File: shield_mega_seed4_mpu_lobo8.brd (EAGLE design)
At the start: 99.4 x 72.4 mm, 37 parts, among them U1 GY-521MPU6050

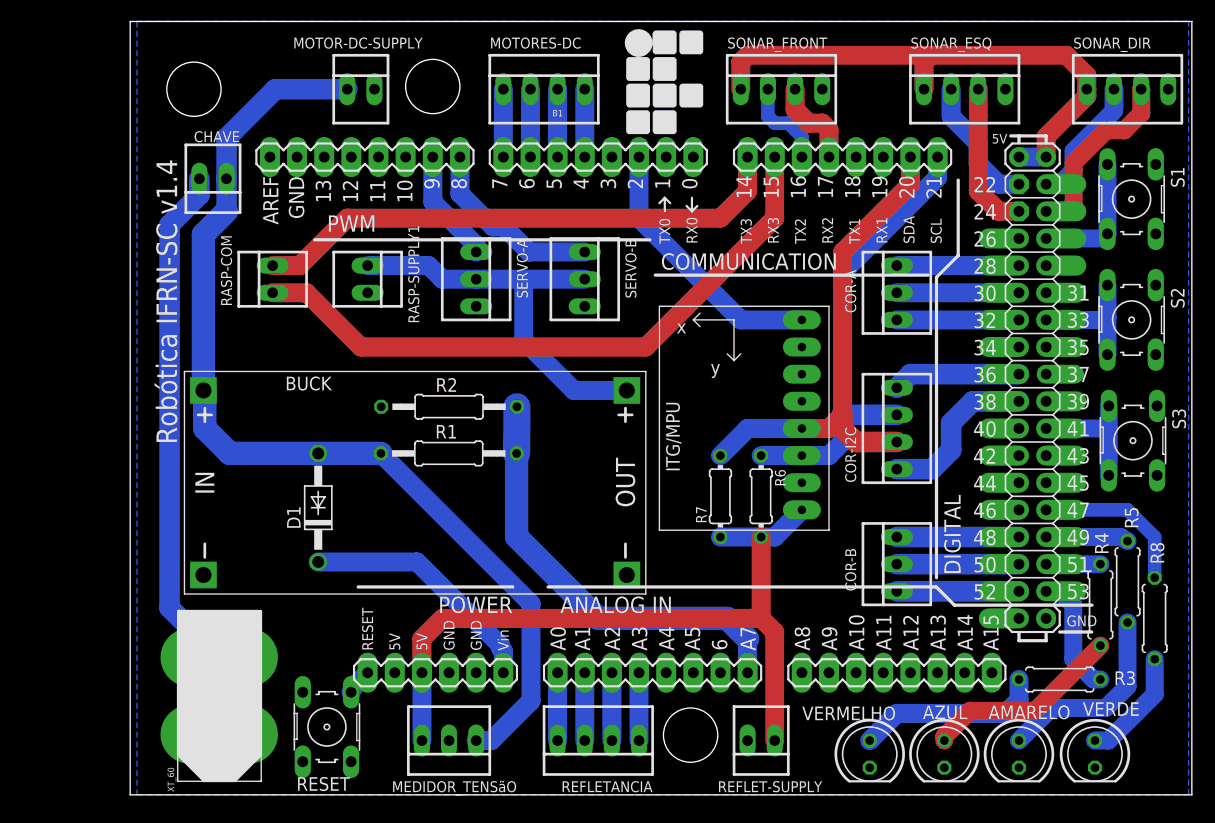
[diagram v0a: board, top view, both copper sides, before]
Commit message: Adição de módulo bluetooth; Remoção do buck; Remoção de conector XT-60; Remoção de conector da chave;
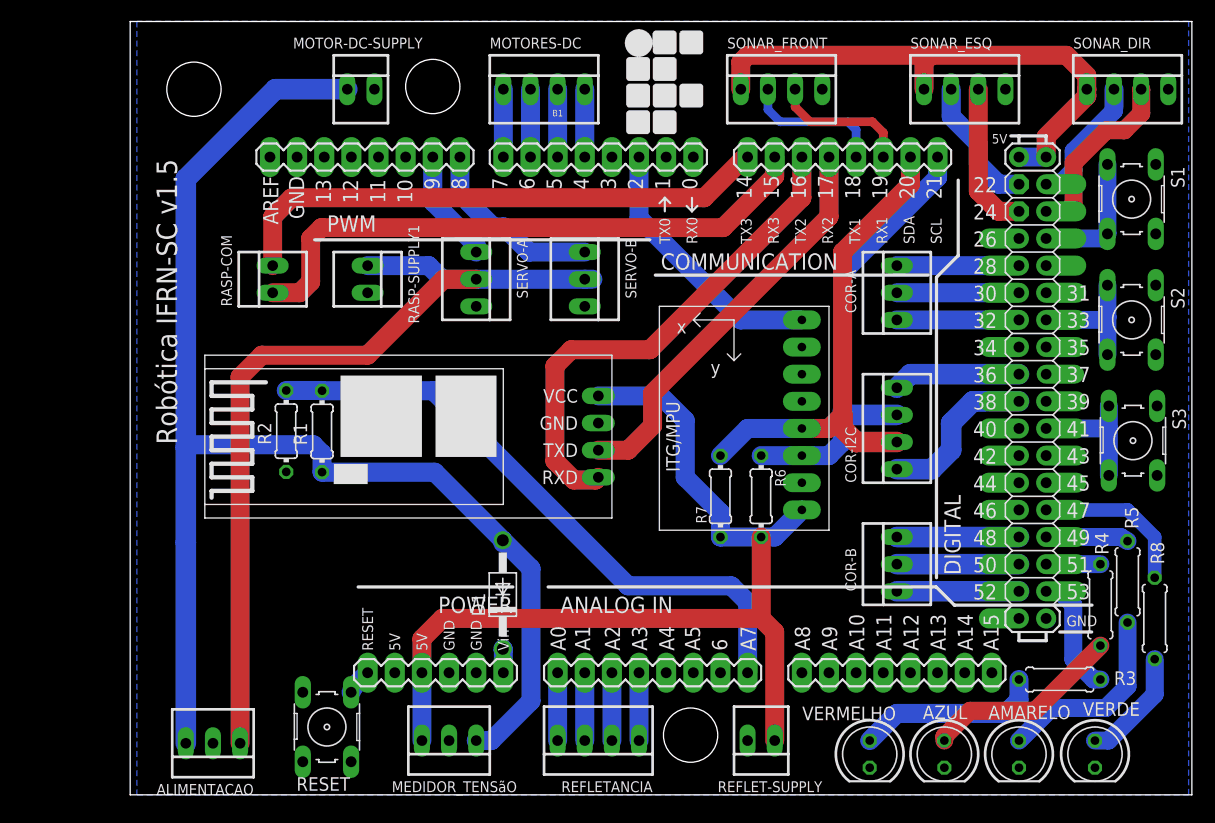
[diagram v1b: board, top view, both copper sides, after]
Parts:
- removed BUCK: (no value), 1484249208697-powermodules:DC-DC-STEP-DOWN-LM2596
- removed CHAVE: (no value), con-molex:22-23-2021
- removed XT_60: (no value), Robotica-IFRN-SC-conectores:XT60
- added ALIMENTACAO: (no value), con-molex:22-23-2031
- added B2: (no value), Bluetooth:BLUETOOTH
- R1, R2: device rcl:0207/12 -> rcl:0204/7
- moved D1 19.1 mm to (34.2, 27.6)
- moved R2 15.4 mm to (14.0, 42.9), turned to 90 degrees
- moved R1 12.0 mm to (17.3, 42.9), turned to 90 degrees
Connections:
- new net N$43: B1.17, B2.2
- net +5V/1: now also B2.4
- net GND: now also ALIMENTACAO.2, B2.3; no longer BUCK.IN-, BUCK.OUT-, XT_60.-
- net N$11: now also B1.19, SONAR_FRONT.3; no longer B1.16, SONAR_FRONT.2
- net N$12: now also B1.18, SONAR_FRONT.2; no longer B1.17, SONAR_FRONT.3
- net N$13: now also B1.16, B2.1; no longer CHAVE.2, XT_60.+
- net VDD: now also ALIMENTACAO.1; no longer BUCK.OUT+
- net VIN: now also ALIMENTACAO.3; no longer BUCK.IN+, CHAVE.1
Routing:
- net VDD: track 38.2 -> 81.8 mm
- net N$43: track 0.00 -> 38.0 mm
- net VIN: track 94.4 -> 129.0 mm
- net +5V/1: track 70.9 -> 92.3 mm
- net N$32: track 23.0 -> 2.26 mm
- net N$20: track 40.9 -> 58.0 mm
- net N$12: track 8.41 -> 13.5 mm
- net N$11: track 8.41 -> 13.2 mm
- net N$10: track 59.8 -> 55.7 mm
- net N$9: track 50.5 -> 51.3 mm
- net N$13: track 47.9 -> 47.2 mm
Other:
- board text added: "Robótica IFRN-SC v1.5"
- board text removed: "Robótica IFRN-SC v1.4"

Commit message: Remoção do conector do multímetro; remoção do conector de alimentação do sensor de refletância; remoção do conector de alimentação do motor;
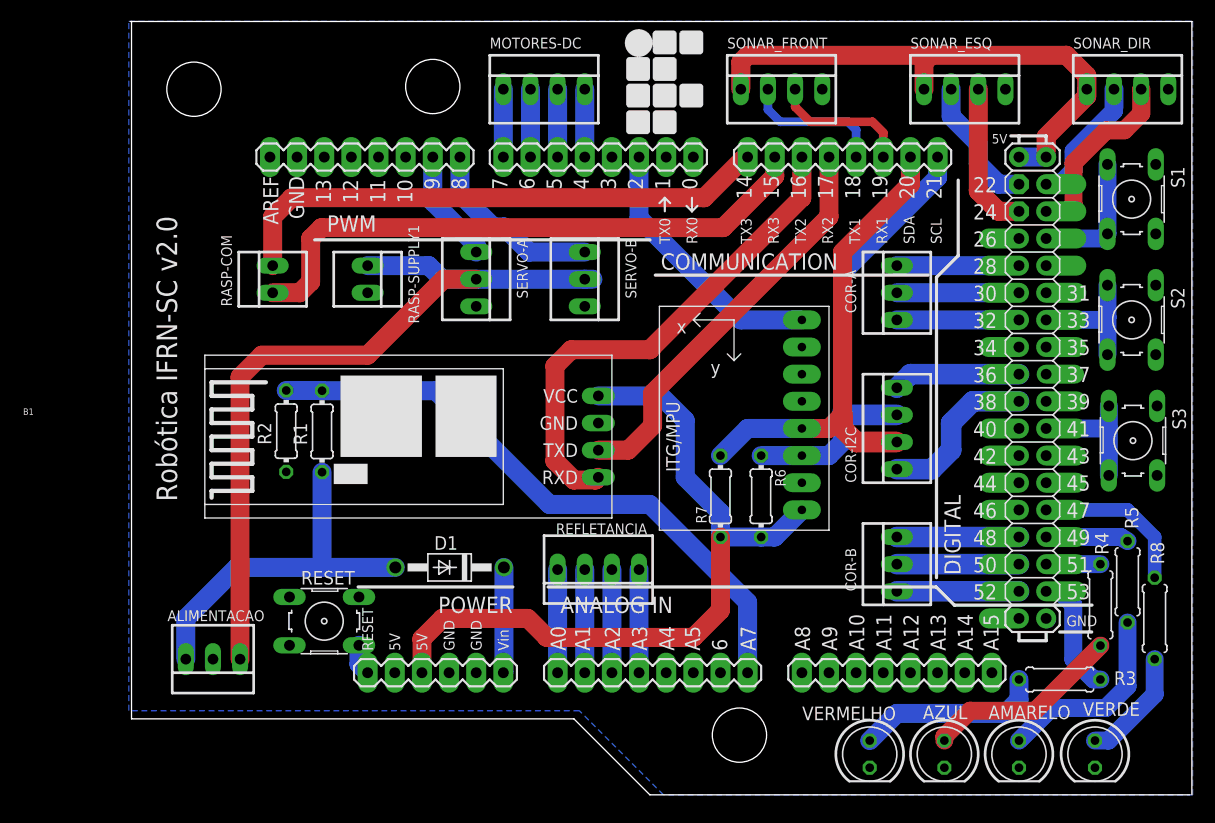
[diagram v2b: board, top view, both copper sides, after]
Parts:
- removed MEDIDOR_TENSãO: (no value), con-molex:22-23-2031
- removed MOTOR-DC-SUPPLY, REFLET-SUPPLY: (no value), con-molex:22-23-2021
- B1: value ARDUINO_MEGA_R3FULL -> (none)
- moved REFLETANCIA 16.0 mm to (43.2, 30.0)
- moved RESET 9.91 mm to (17.5, 25.1), turned to 180 degrees
- moved ALIMENTACAO 7.87 mm to (7.11, 21.6)
- moved D1 5.59 mm to (29.3, 30.2), turned to 180 degrees
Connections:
- net +5V/1: no longer MEDIDOR_TENSãO.3, REFLET-SUPPLY.1
- net GND: no longer MEDIDOR_TENSãO.2, MOTOR-DC-SUPPLY.2, RASP-SUPPLY1.2, REFLET-SUPPLY.2
- net VIN: no longer MEDIDOR_TENSãO.1, MOTOR-DC-SUPPLY.1
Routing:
- net VIN: track 129.0 -> 34.4 mm
- net +5V/1: track 92.3 -> 70.6 mm
- net VDD: track 81.8 -> 73.9 mm
- net N$32: track 2.26 -> 9.88 mm
- net N$33: track 6.35 -> 9.65 mm
- net N$29: track 6.35 -> 9.65 mm
- net N$2: track 6.35 -> 9.65 mm
- net N$1: track 6.35 -> 9.65 mm
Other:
- outline, holes or cut-outs redrawn
- board text added: "Robótica IFRN-SC v2.0"
- board text removed: "Robótica IFRN-SC v1.5"

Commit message: remoção de erro que deixou o conector de alimentação sem terra
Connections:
- net GND: now also RASP-SUPPLY1.2
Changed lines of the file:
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@@
 <layer number="20" name="Dimension" color="15" fill="1" visible="yes" active="yes"/>
 <layer number="21" name="tPlace" color="7" fill="1" visible="yes" active="yes"/>
-<layer number="22" name="bPlace" color="7" fill="1" visible="yes" active="yes"/>
+<layer number="22" name="bPlace" color="7" fill="1" visible="no" active="yes"/>
 <layer number="23" name="tOrigins" color="15" fill="1" visible="yes" active="yes"/>
 <layer number="24" name="bOrigins" color="15" fill="1" visible="yes" active="yes"/>
@@
 <vertex x="-0.762" y="16.764"/>
 </polygon>
+<contactref element="RASP-SUPPLY1" pad="2"/>
 </signal>
 <signal name="VIN">

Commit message: Adição de terra em pino do botão de reset que estava faltando
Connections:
- net GND: now also RESET.4
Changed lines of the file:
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@@
 </polygon>
 <contactref element="RASP-SUPPLY1" pad="2"/>
+<contactref element="RESET" pad="4"/>
+<wire x1="20.7772" y1="27.4066" x2="14.2748" y2="27.4066" width="0" layer="19" extent="1-1"/>
 </signal>
 <signal name="VIN">

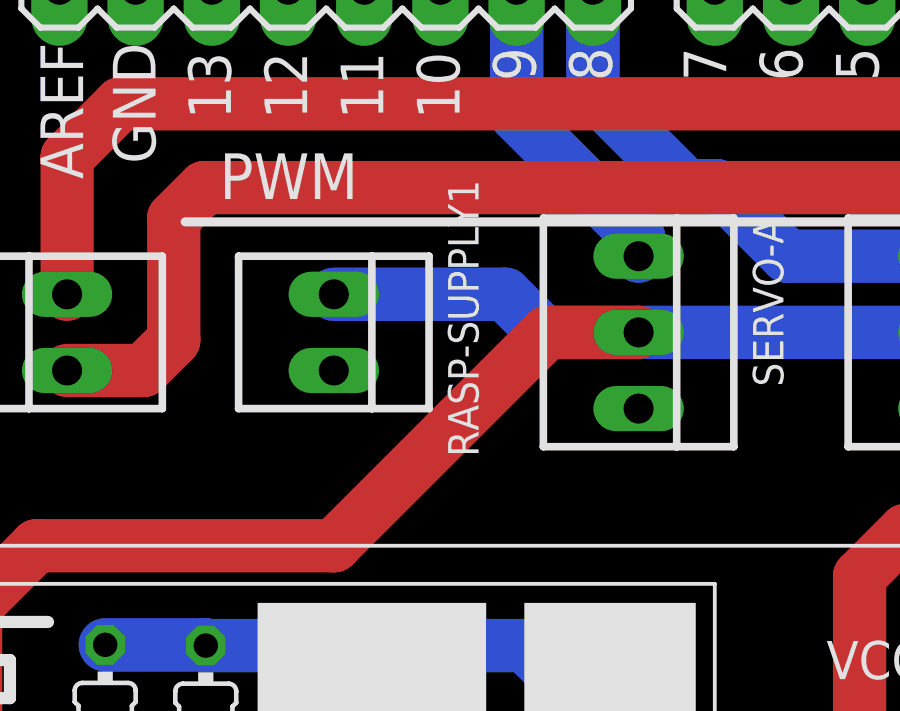
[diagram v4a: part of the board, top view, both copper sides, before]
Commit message: Remoção do conector de alimentação do raspberry PI
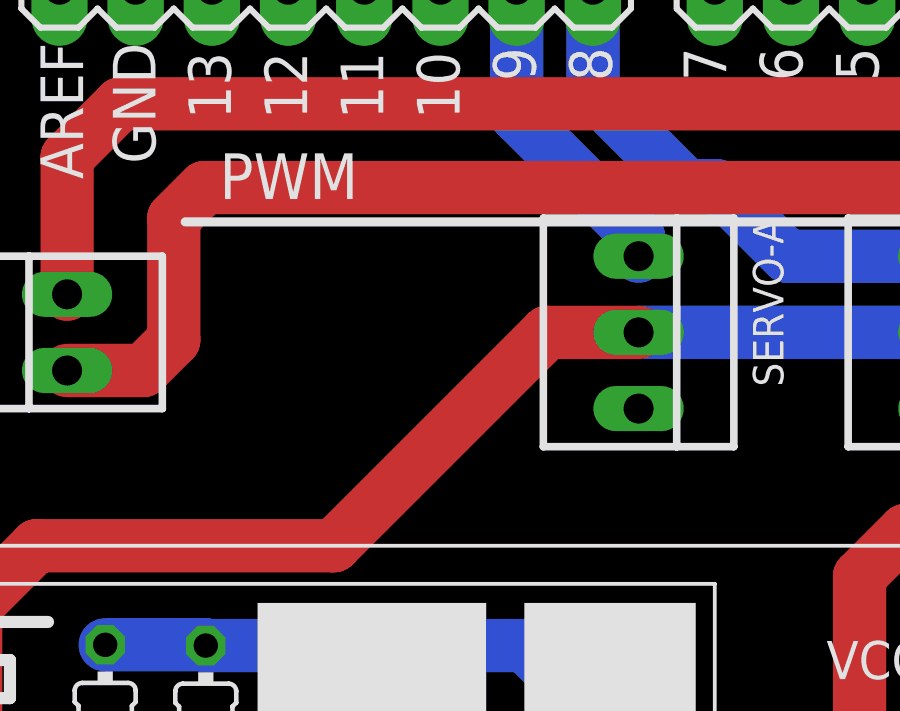
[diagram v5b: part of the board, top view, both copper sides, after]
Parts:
- removed RASP-SUPPLY1: (no value), con-molex:22-23-2021
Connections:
- net GND: no longer RASP-SUPPLY1.2
- net VDD: no longer RASP-SUPPLY1.1
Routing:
- net VDD: track 73.9 -> 63.2 mm
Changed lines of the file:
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@@
 <attribute name="OC_FARNELL" value="1462920" x="38.1" y="74.93" size="1.778" layer="27" display="off"/>
-</element>
-<element name="RASP-SUPPLY1" library="con-molex" package="22-23-2021" value="" x="21.59" y="57.15" smashed="yes" rot="R270">
-<attribute name="OC_NEWARK" value="25C3832" x="21.59" y="57.15" size="1.778" layer="27" rot="R270" display="off"/>
-<attribute name="MPN" value="22-23-2021" x="21.59" y="57.15" size="1.778" layer="27" rot="R270" display="off"/>
-<attribute name="MF" value="MOLEX" x="21.59" y="57.15" size="1.778" layer="27" rot="R270" display="off"/>
-<attribute name="OC_FARNELL" value="1462926" x="21.59" y="57.15" size="1.778" layer="27" rot="R270" display="off"/>
-<attribute name="NAME" x="25.4" y="62.23" size="1.016" layer="25" ratio="10" rot="R270"/>
-<attribute name="VALUE" x="16.51" y="59.69" size="1.016" layer="27" ratio="10" rot="R270"/>
 </element>
 <element name="RASP-COM" library="con-molex" package="22-23-2021" value="" x="12.7" y="57.15" rot="R90">
@@
 <vertex x="-0.762" y="16.764"/>
 </polygon>
-<contactref element="RASP-SUPPLY1" pad="2"/>
 <contactref element="RESET" pad="4"/>
-<wire x1="20.7772" y1="27.4066" x2="14.2748" y2="27.4066" width="0" layer="19" extent="1-1"/>
 </signal>
 <signal name="VIN">
@@
 <contactref element="SERVO-A" pad="2"/>
 <contactref element="SERVO-B" pad="2"/>
-<contactref element="RASP-SUPPLY1" pad="1"/>
-<wire x1="21.59" y1="58.42" x2="27.305" y2="58.42" width="1.778" layer="16"/>
-<wire x1="27.305" y1="58.42" x2="28.575" y2="57.15" width="1.778" layer="16"/>
-<wire x1="28.575" y1="57.15" x2="31.75" y2="57.15" width="1.778" layer="16"/>
 <contactref element="ALIMENTACAO" pad="1"/>
 <wire x1="9.652" y1="48.006" x2="11.684" y2="50.038" width="1.778" layer="1"/>

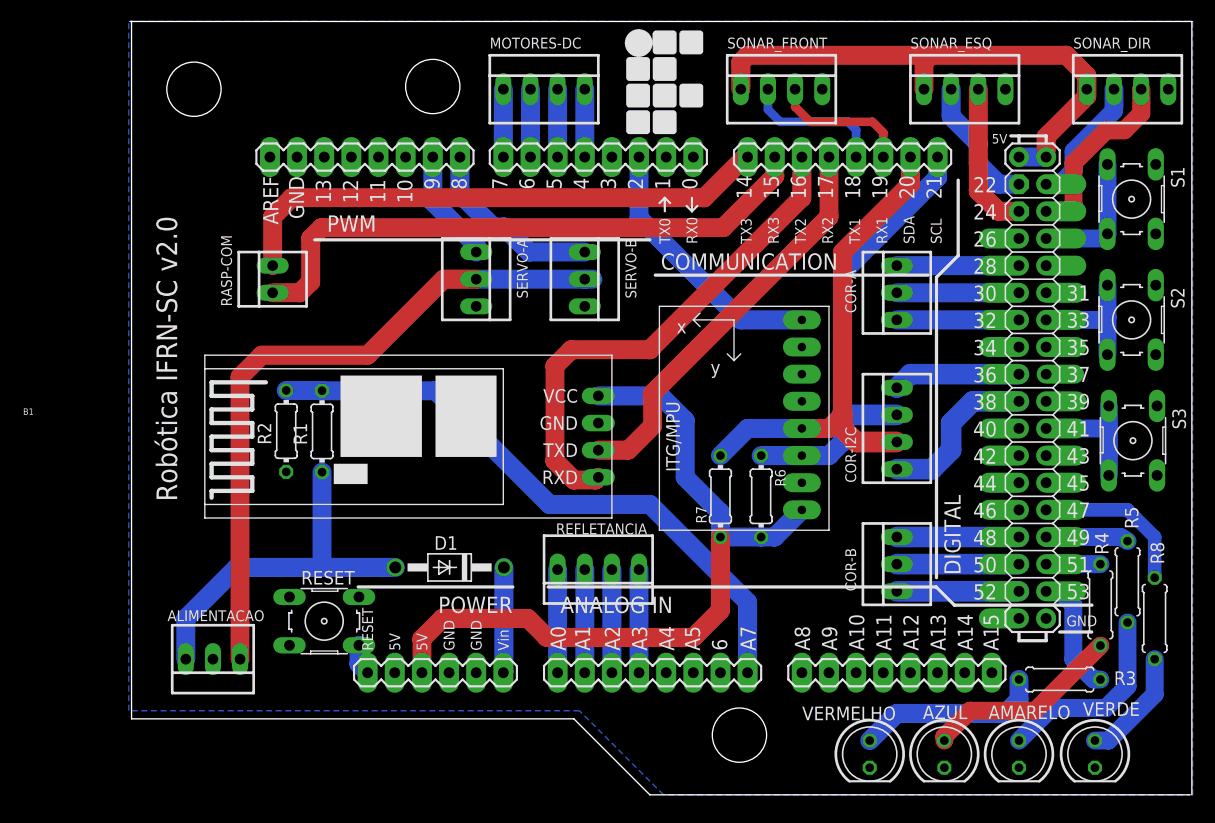
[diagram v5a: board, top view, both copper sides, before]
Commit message: Modificação de posição do conector do motor e conectores dos servo motores; modificação de posição do símbolo do IF
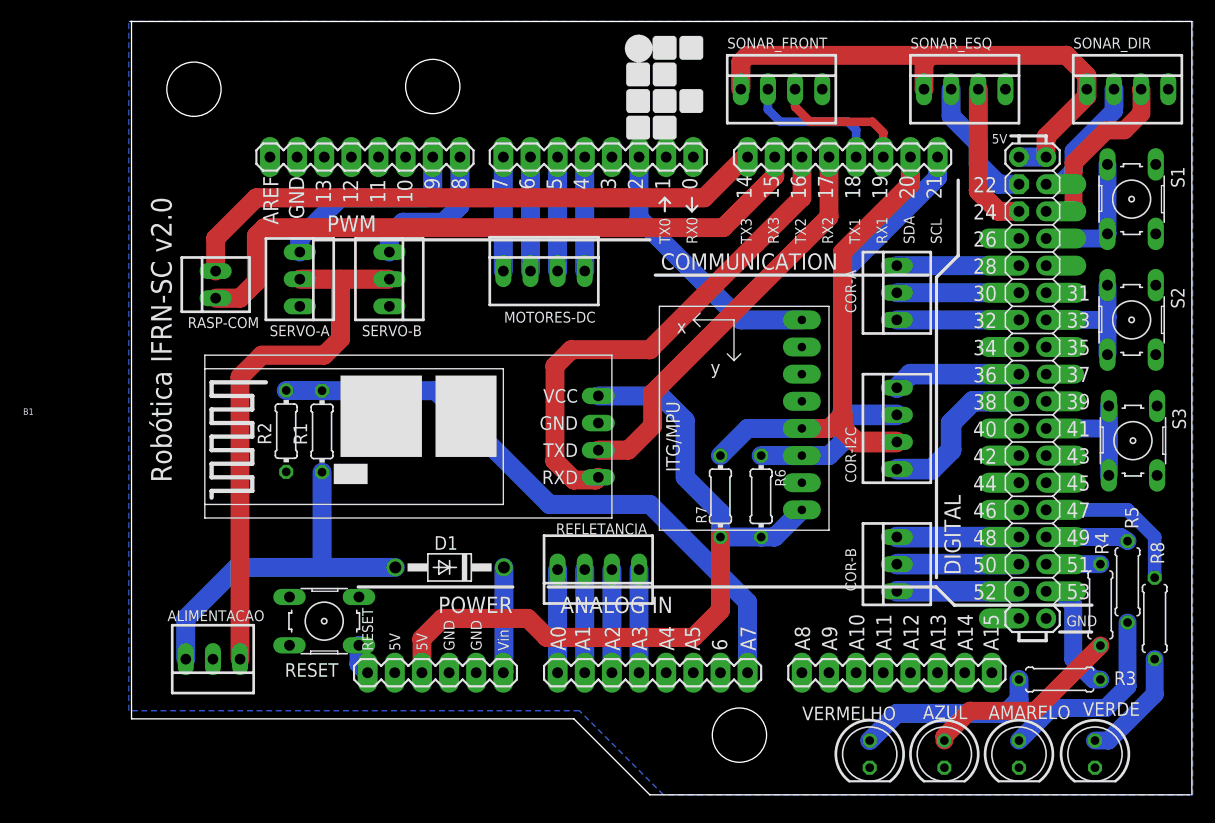
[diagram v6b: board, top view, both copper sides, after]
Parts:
- moved SERVO-B 18.3 mm to (23.6, 57.1)
- moved MOTORES-DC 17.0 mm to (38.1, 57.9)
- moved SERVO-A 16.5 mm to (15.2, 57.1)
- moved RASP-COM 5.36 mm to (7.37, 56.6)
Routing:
- net VDD: track 63.2 -> 51.3 mm
- net N$8: track 10.6 -> 18.8 mm
- net N$10: track 55.7 -> 61.4 mm
- net N$9: track 51.3 -> 56.0 mm
- net N$6: track 6.35 -> 10.7 mm
- net N$5: track 6.35 -> 10.7 mm
- net N$4: track 6.35 -> 10.7 mm
- net N$3: track 6.35 -> 10.7 mm
- net N$7: track 17.4 -> 13.9 mm
